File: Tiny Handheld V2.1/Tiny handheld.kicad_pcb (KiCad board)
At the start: 2 copper layers, 34.3 x 58.4 mm, 42 parts, among them IC1 BQ21040DBVR, J1 VDisplay/prog1, J2 HDisplay/prog, J3 USB_C_Receptacle_USB2.0, U1 ATtiny85-20P, U2 ATtiny85-20S

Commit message: stopped for now.
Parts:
- removed 5V: 5V, TestPoint:TestPoint_Pad_1.0x1.0mm
- removed GND: GND, TestPoint:TestPoint_Pad_1.0x1.0mm
- added 5V1: 5V, TestPoint:TestPoint_Pad_1.0x1.0mm, F.Cu at (144.2, 108.4)
- added C1: 1uF 16V, Capacitor_SMD:C_1206_3216Metric_Pad1.33x1.80mm_HandSolder, F.Cu at (145.6, 105.2)
- added GND1: GND, TestPoint:TestPoint_Pad_1.0x1.0mm, F.Cu at (150.2, 105.0)
- renumbered en-charge to en-charge1
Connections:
- S2 pad 7: GND -> (no net)
- S2 pad 8: GND -> (no net)
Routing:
- net PB2/SCL/SCK: track 63.9 -> 100.2 mm, vias 5 -> 9
- net Net-(C6-Pad1): track 36.3 -> 0.00 mm, vias 4 -> 0
- net Net-(R5-Pad2): track 48.7 -> 15.3 mm
- net Net-(R3-Pad2): track 33.5 -> 23.8 mm
- net Net-(R1-Pad2): track 13.8 -> 6.72 mm
- net Net-(R4-Pad2): track 14.3 -> 10.5 mm
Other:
- board text added: "TODO: Fix 5 way button (DONE) Enlarge keyhole smaller battery holder? rewire"

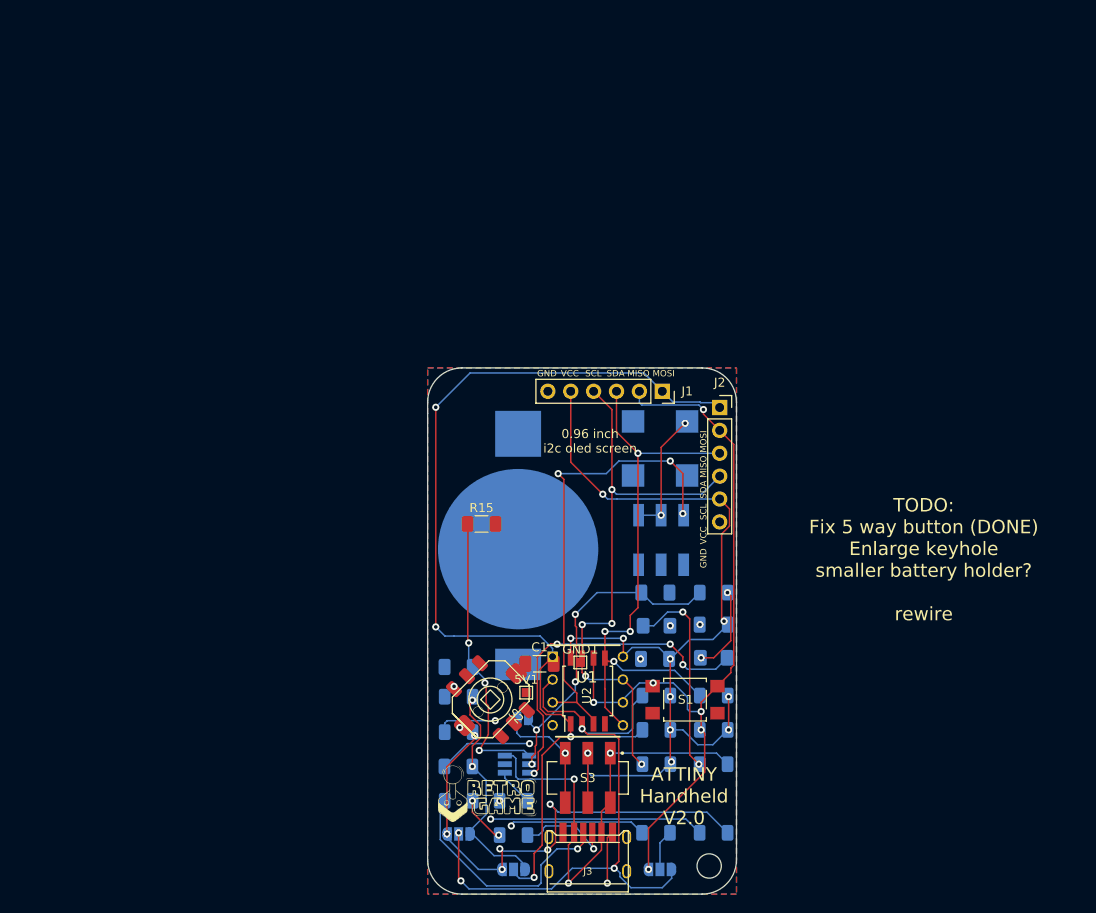
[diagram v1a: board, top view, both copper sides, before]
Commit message: enh v2.1
- new 5 way button footprint (functional)
- larger keyhole
- rewired
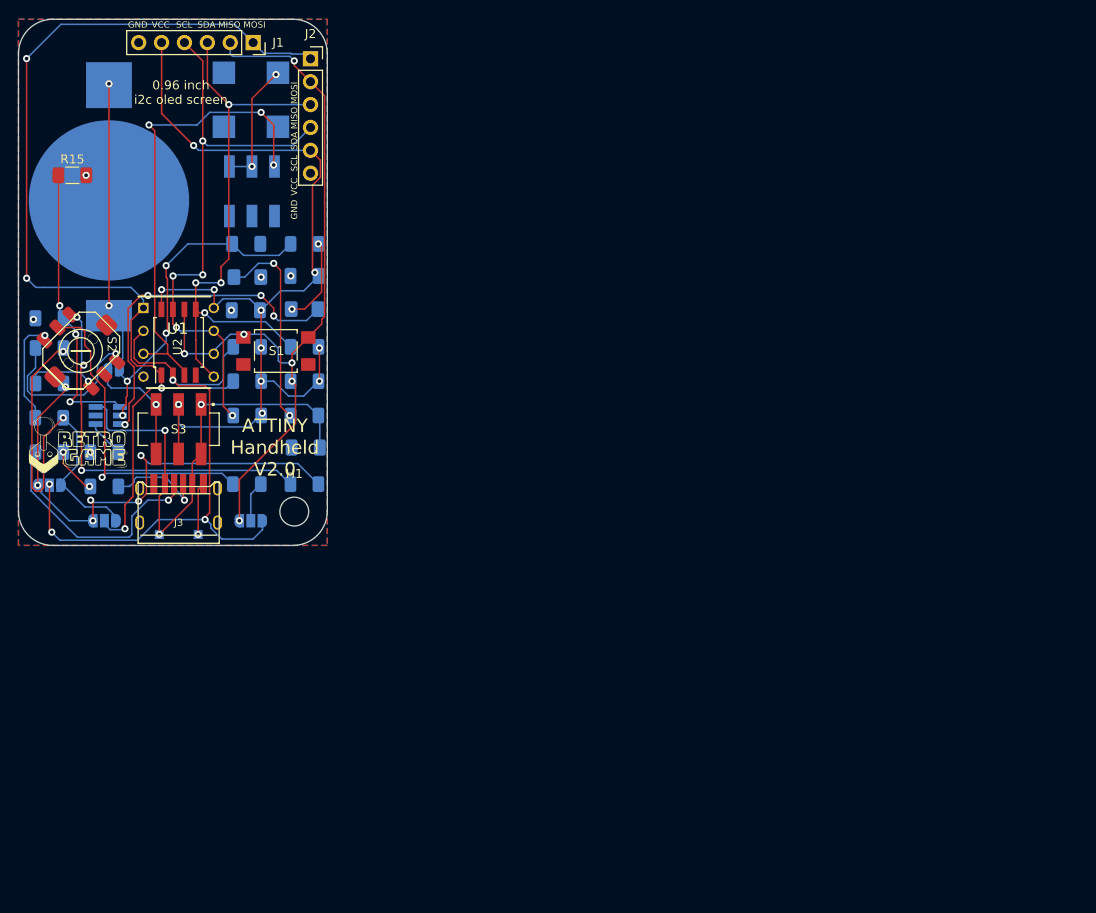
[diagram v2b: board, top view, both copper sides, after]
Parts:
- removed REF**: MountingHole_2.7mm_M2.5_ISO7380, MountingHole:MountingHole_2.7mm_M2.5_ISO7380
- removed en-charge1: Jumper_2_Open, Jumper:SolderJumper-2_P1.3mm_Open_RoundedPad1.0x1.5mm
- added H1: MountingHole, MountingHole:MountingHole_3.2mm_M3, F.Cu at (118.4, 88.3)
- added en-chrg1: Jumper_2_Open, Jumper:SolderJumper-2_P1.3mm_Open_RoundedPad1.0x1.5mm, B.Cu at (98.3, 72.5)
- 5V1, C1, GND1: moved to B.Cu
- BT1: value BATTERY-6.8MM_SMD -> Battery_Cell
- moved S2 60.1 mm to (94.8, 70.5), turned to 0 degrees
- moved C4 59.7 mm to (113.0, 65.9)
- moved D2 59.7 mm to (119.5, 65.8)
- moved J1 59.7 mm to (113.8, 36.2)
- moved J2 59.7 mm to (120.2, 38.0)
- moved LS1 59.7 mm to (113.6, 42.6)
- moved R10 59.7 mm to (119.5, 73.8)
- moved R12 59.7 mm to (119.5, 70.0)
- moved R15 59.7 mm to (93.8, 51.0)
- moved R2 59.7 mm to (113.2, 70.0)
- moved R4 59.7 mm to (91.2, 77.9)
- moved R6 59.7 mm to (113.2, 73.8)
- moved BT1 59.7 mm to (97.8, 53.7)
- moved C3 59.7 mm to (119.5, 62.1)
- moved C6 59.7 mm to (113.1, 58.6)
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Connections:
- BT1 pad 1: (no net) -> BatOut
- BT1 pad 2: (no net) -> GND
- S2 pad DOWN: (no net) -> Net-(R1-Pad2)
- S2 pad LEFT: (no net) -> Net-(R4-Pad2)
- S2 pad RIGHT: (no net) -> Net-(R7-Pad2)
- S2 pad UP: (no net) -> Net-(R3-Pad2)
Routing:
- net PB2/SCL/SCK: track 100.2 -> 63.9 mm, vias 9 -> 5
- net Net-(C6-Pad1): track 0.00 -> 36.3 mm, vias 0 -> 4
- net BatOut: track 13.4 -> 45.8 mm, vias 1 -> 3
- net Net-(R5-Pad2): track 15.3 -> 35.7 mm
- net Net-(JP1-Pad1): track 25.2 -> 44.0 mm
- net Net-(R3-Pad2): track 23.8 -> 41.3 mm, vias 1 -> 3
- net Net-(R7-Pad2): track 1.47 -> 18.1 mm
- net ExtVCC: track 50.9 -> 54.6 mm
- net Net-(R4-Pad2): track 10.5 -> 11.6 mm
- net Net-(R1-Pad2): track 6.72 -> 7.39 mm
- net GND: vias 8 -> 9
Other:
- board text removed: "TODO: Fix 5 way button (DONE) Enlarge keyhole smaller battery holder? rewire"

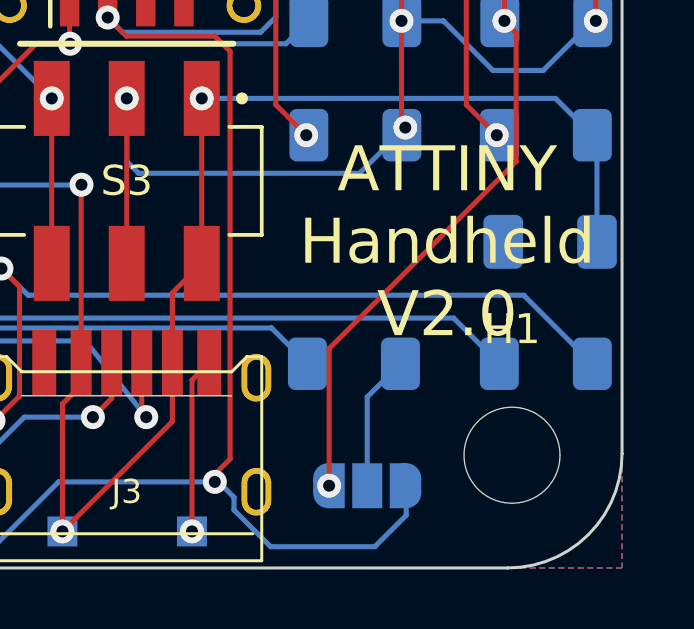
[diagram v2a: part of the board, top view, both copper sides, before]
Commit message: Improved silkscreen
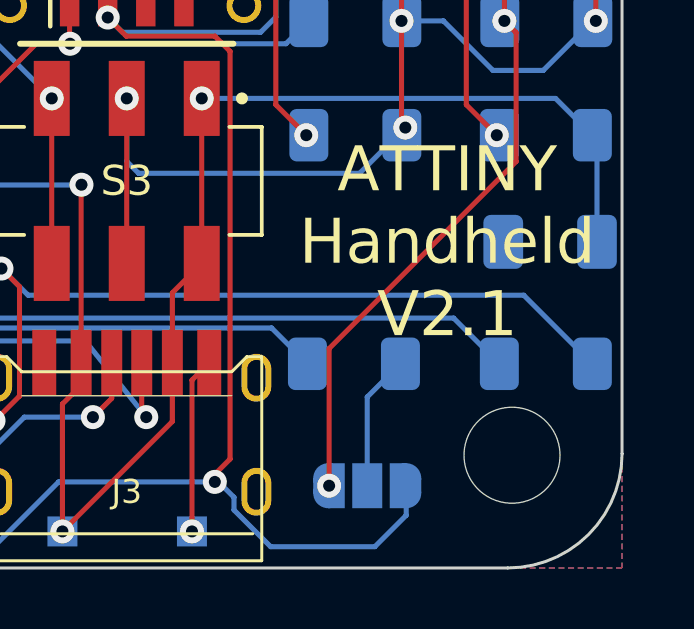
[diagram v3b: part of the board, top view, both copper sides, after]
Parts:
- added REF**: OSHW-Logo2_7.3x6mm_SilkScreen, Symbol:OSHW-Logo2_7.3x6mm_SilkScreen, B.Cu at (105.5, 70.1)
- renumbered 5V1 to 5V, GND1 to GND, en-chrg1 to en-charge
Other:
- board text added: "5V USB PWR"
- board text added: "ATTINY Handheld V2.1"
- board text added: "PWR"
- board text added: "sound"
- board text removed: "5V usb External power"
- board text removed: "ATTINY Handheld V2.0"

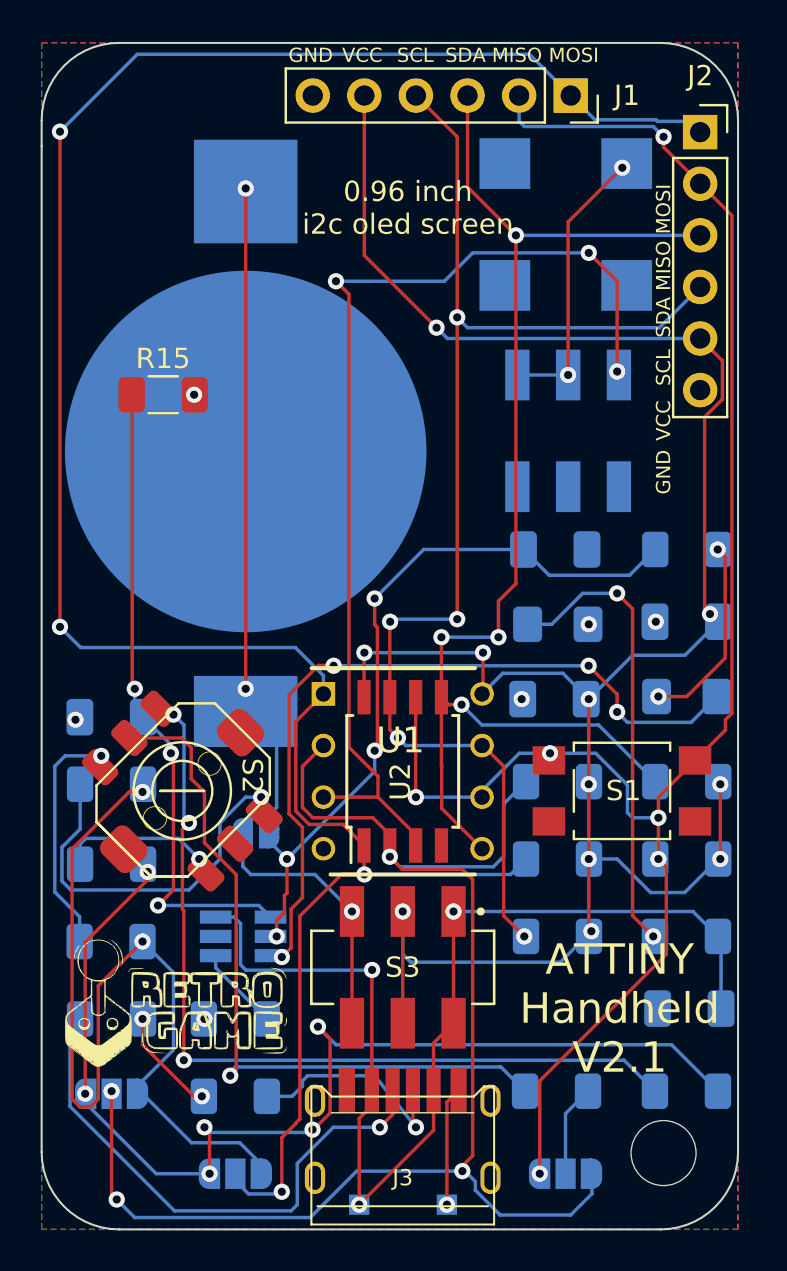
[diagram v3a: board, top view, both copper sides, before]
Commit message: improved silkscreen and archieved 3d models
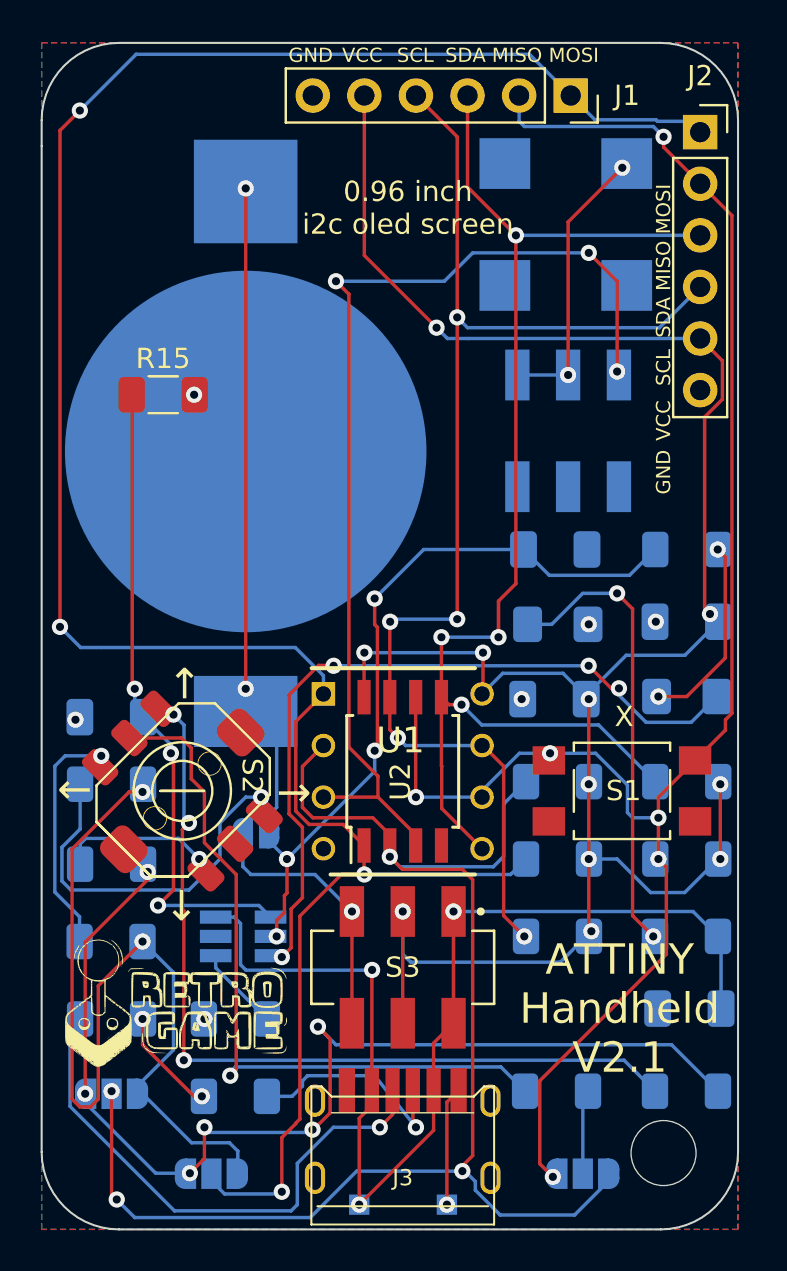
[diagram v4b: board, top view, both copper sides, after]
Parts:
- moved JP2 1.18 mm to (96.1, 89.3)
- moved JP3 0.85 mm to (114.4, 89.3)
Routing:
- net PB5/RES: track 115.0 -> 116.2 mm
- net Net-(JP1-Pad1): track 44.0 -> 43.3 mm
- net Net-(JP1-Pad3): track 54.8 -> 54.0 mm
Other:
- board text added: "X"
- board text added: "←"

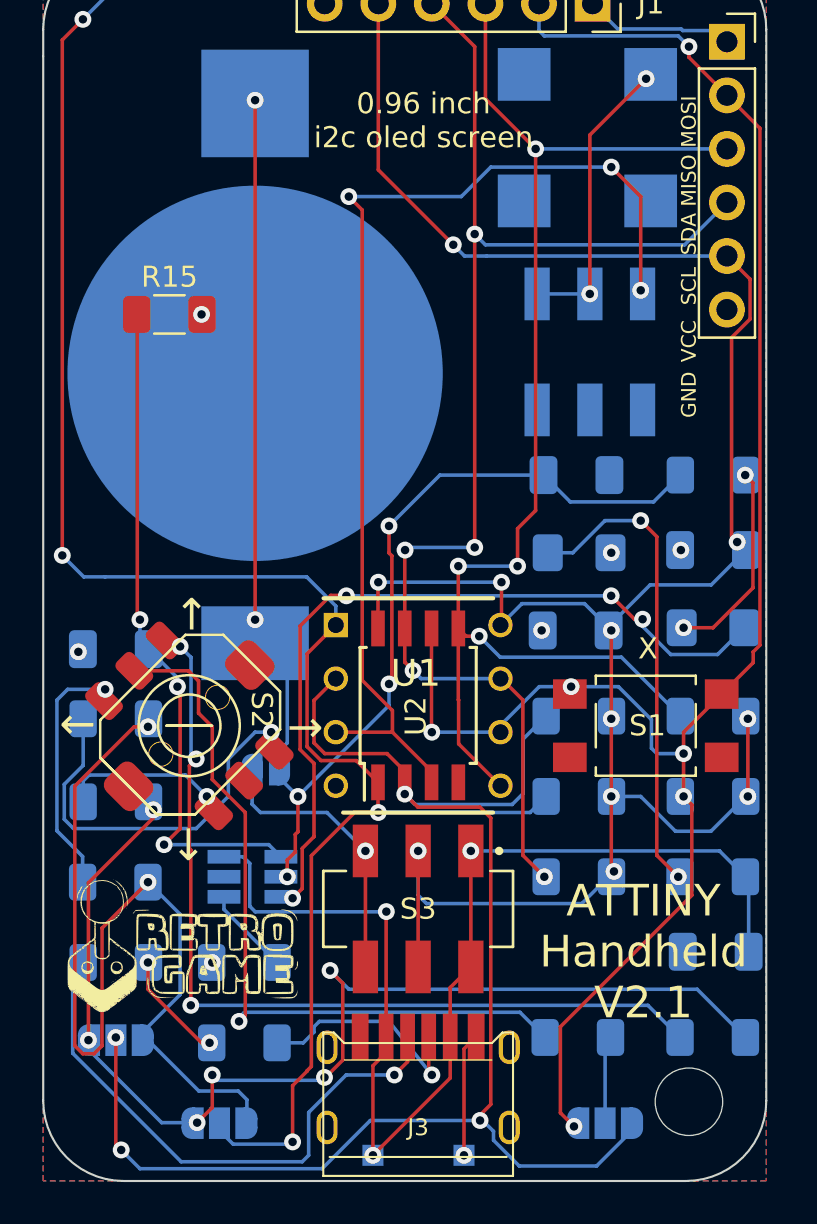
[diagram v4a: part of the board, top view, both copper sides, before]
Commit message: Improved wiring spacing
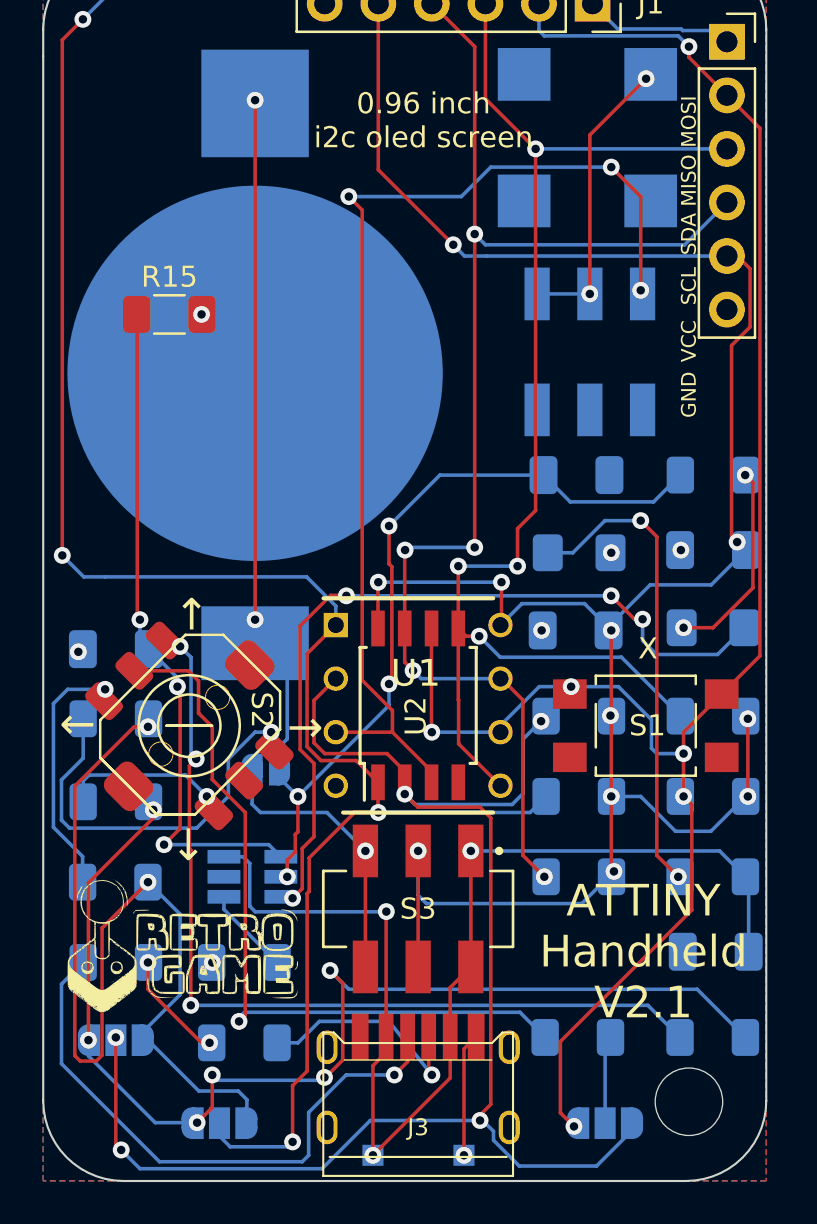
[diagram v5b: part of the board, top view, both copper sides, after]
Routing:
- net Net-(J3-PadA5): track 26.9 -> 27.9 mm
- net Net-(JP1-Pad1): track 43.3 -> 44.1 mm
- net PB3: vias 4 -> 5

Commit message: small improvements V2.1
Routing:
- net PB5/RES: track 116.4 -> 114.8 mm
- net VCC: track 105.9 -> 104.4 mm
- net PB3: track 71.9 -> 70.4 mm
- net PB1/MISO: track 85.9 -> 84.4 mm
- net Net-(JP1-Pad1): track 44.1 -> 43.0 mm
- net Net-(J3-PadA5): track 27.9 -> 27.0 mm
- net Net-(JP1-Pad3): track 54.2 -> 53.3 mm
- net PB2/SCL/SCK: track 63.9 -> 63.1 mm
- net PB0/SDA/MOSI: track 63.4 -> 62.6 mm
- net Net-(D2-Pad1): track 37.5 -> 36.9 mm
- net Net-(C6-Pad1): track 36.3 -> 35.6 mm
- net Net-(R7-Pad2): track 18.3 -> 17.7 mm
- net Net-(R5-Pad2): track 35.7 -> 35.1 mm
- net PB4: track 51.5 -> 52.1 mm
- net ExtVCC: track 54.6 -> 54.0 mm

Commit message: V2.2 started (minor bug fixes)
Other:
- board text added: "TO DO: fix silkscreen error on com port (MISO / MOSI)"
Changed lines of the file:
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@@
   (title_block
     (title "Tiny Handheld")
-    (date "2022-11-21")
-    (rev "2.1")
+    (date "2022-12-04")
+    (rev "2.2")
     (comment 1 "Casper R. Tak")
   )
@@
     (effects (font (size 1.5 1.5) (thickness 0.2)))
   )
+  (gr_text "TO DO:\nfix silkscreen error on com port (MISO / MOSI)" (at 164 36.25) (layer "F.SilkS")
+    (effects (font (size 1.5 1.5) (thickness 0.3)))
+  )
   (gr_text "←" (at 100.203 70.612 180) (layer "F.SilkS")
